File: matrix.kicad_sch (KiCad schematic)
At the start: 153 parts

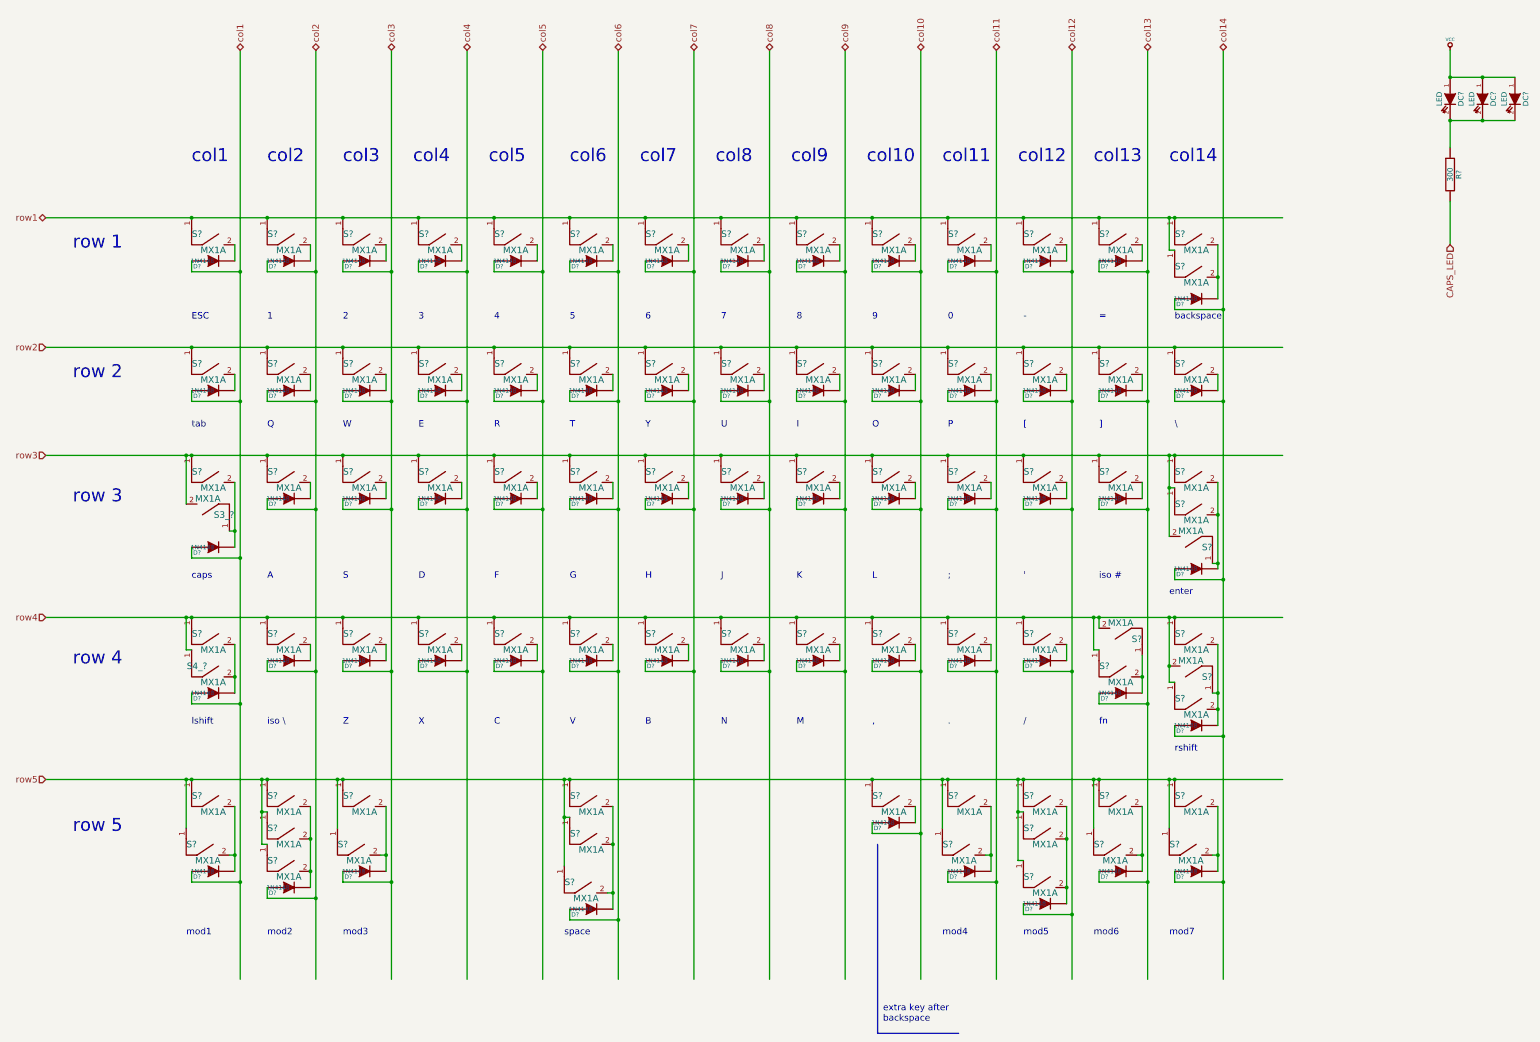
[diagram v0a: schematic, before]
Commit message: add gh60 lib to project
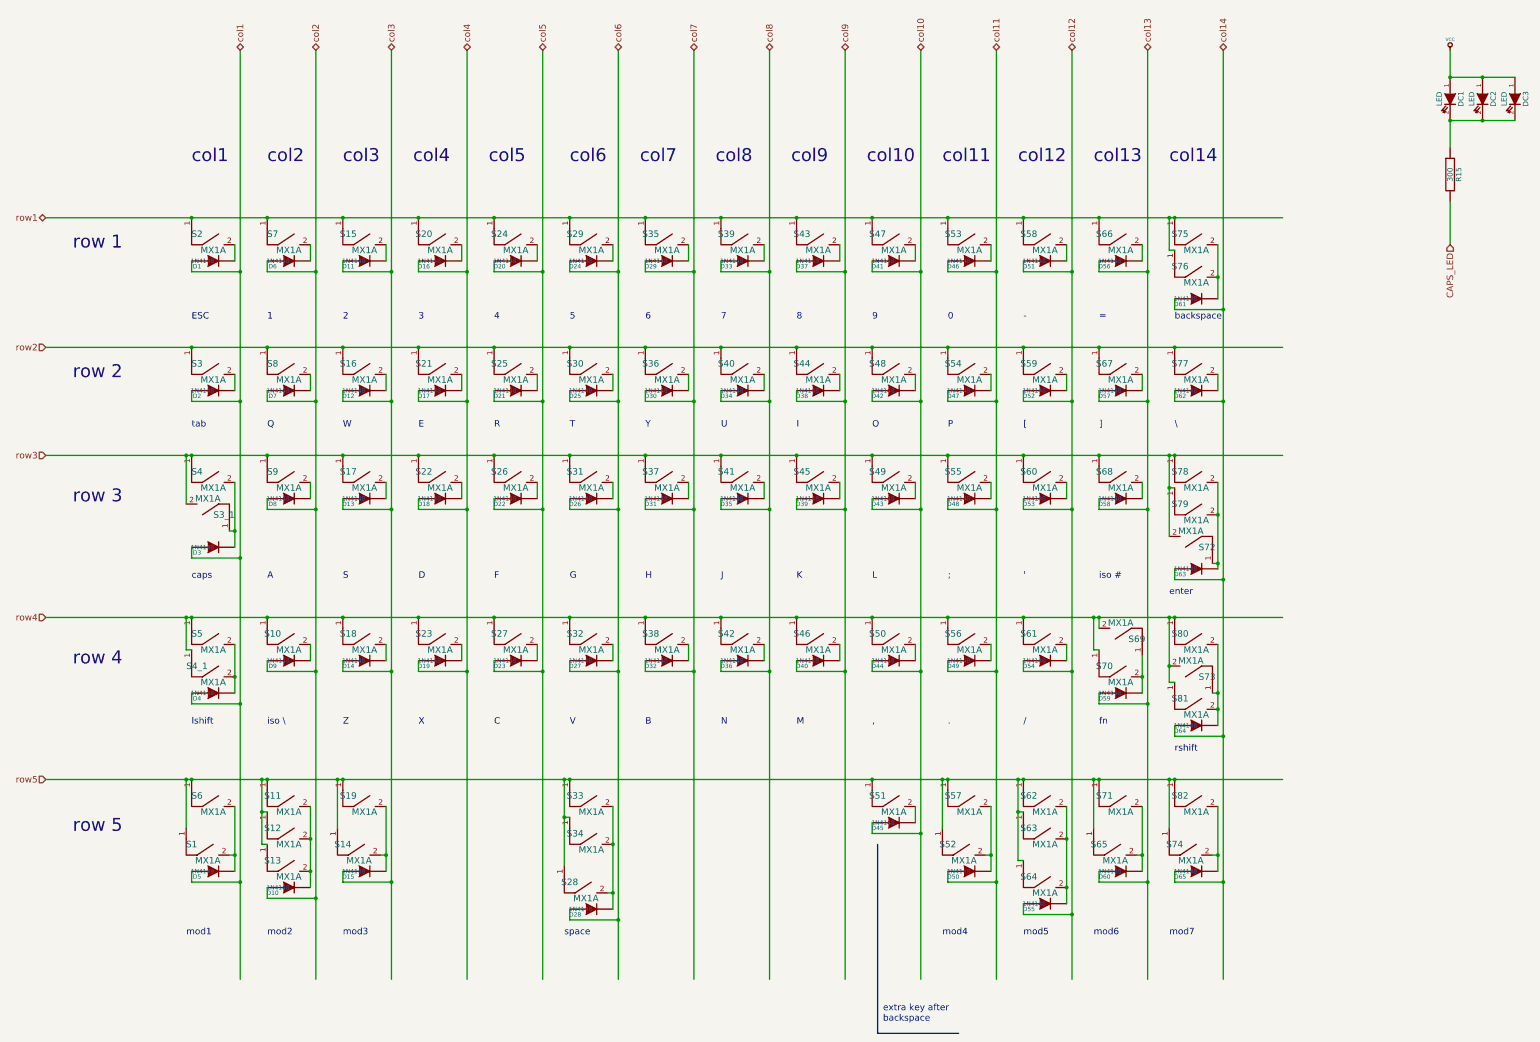
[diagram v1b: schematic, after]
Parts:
- gave numbers to parts that had none: 153
